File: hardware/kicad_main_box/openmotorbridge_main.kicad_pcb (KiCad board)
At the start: 4 copper layers, 85 x 55 mm, 41 parts, among them J1 DEUTSCH_DTM12_IDC_HEADER, J2 MicroSD_Card, J3 USB2_IDC_HEADER_9PIN, J4 RGB_LED_3PIN, J5 PWR_BAT_NTC_4PIN, SW1 SW_PAIR_RESET, U1 LM5164-Q1, U10 SX1262IMLTRT, U11 TPS7A0533_LDO, U2 ESP32-S3-WROOM-1U-N16R8, U3 ES8388_Codec, U5 BMI270_IMU, U6 TCAN334G, U8 DW3110, U9 QCC3084_BT54_AUDIO, Y1_UWB 38.4MHz

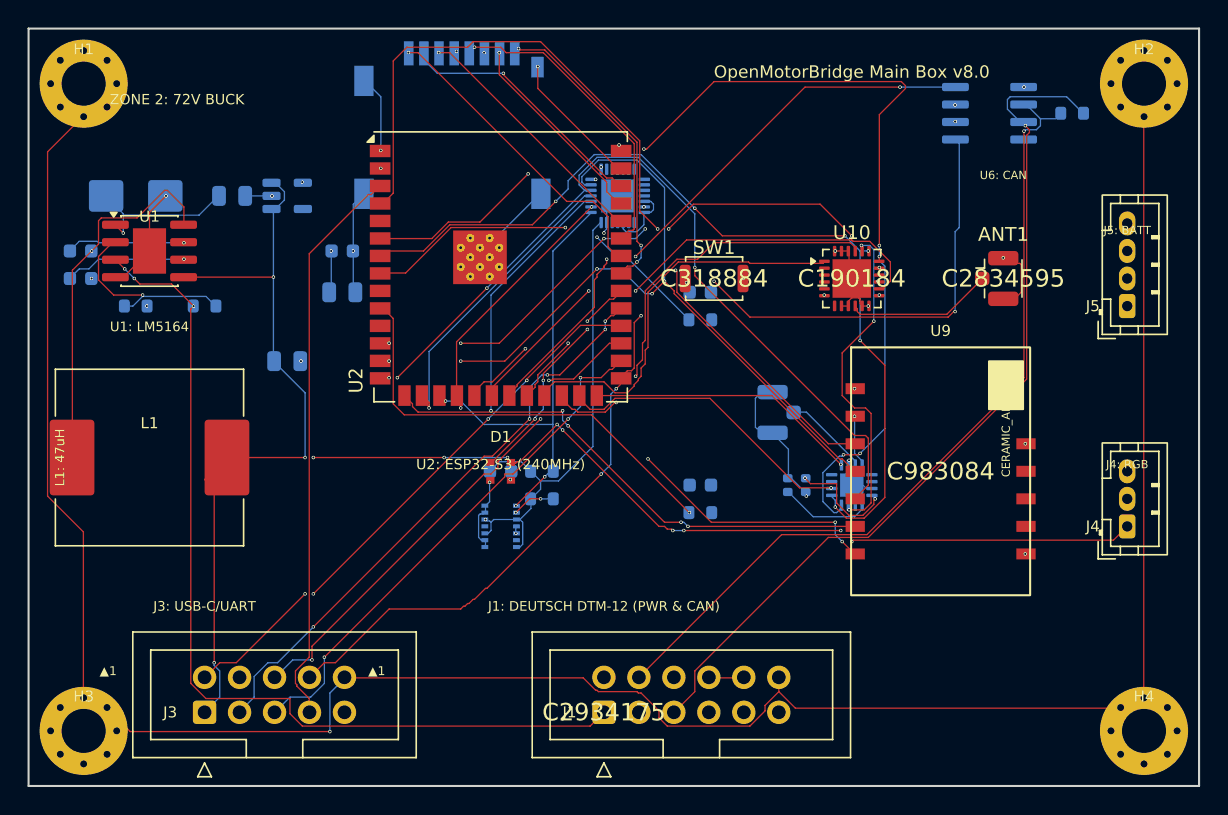
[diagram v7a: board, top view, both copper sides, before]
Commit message: feat(hw): finalize PCB lineup routing, sync PCBA 03 cartridge with J_PROG header and DTM12 schematics
- PCBA 01 (Central Box): Remediate net routing, DTM12 hierarchical schematic synchronization, 100% routed, 0 DRC errors.
- PCBA 03 (Smart Modular Cartridge): Position and route J_PROG 4-pin SMD programming header on F.Cu at (108.0, 89.61), synchronize CPL and schematic, 100% routed, 0 DRC errors.
- PCBA 05 (Universal Front Node): Preconnect and routing verified, 100% routed, 0 DRC errors.
- PCBA 07 (LoRa Smart-Keyfob): Routing and DRC verified, 100% routed, 0 DRC errors.
- PCBA 08 (Radar 2.0 Sub-MCU & Wings): Sub-MCU routing and HF isolation verified, 100% routed, 0 DRC errors.
- PCBA 10 (OMM 446 PMR/DMR Intercom): KiCad DRC verified, 100% routed, 0 DRC errors.
- Firmware: Align configuration headers across front_node and smart_cartridge.
- Tools: Add comprehensive preflight PCBA audit suite tools/audit_pcbas_preflight.py.
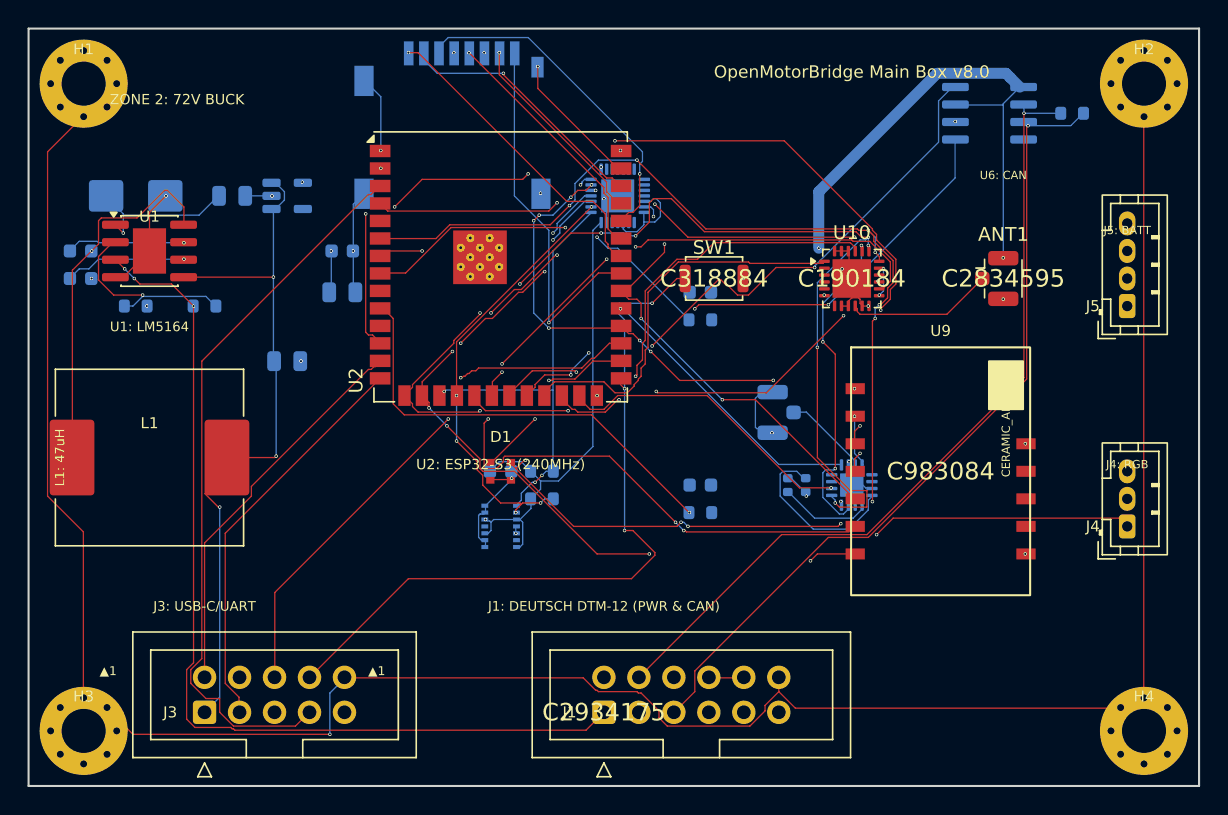
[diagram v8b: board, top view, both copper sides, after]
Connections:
- U2 pad 13: I2S_BCLK -> USB_D_N
- U2 pad 14: I2S_WS -> USB_D_P
- U2 pad 26: UWB_IRQ -> GND_PWR
- U2 pad 28: UART_TXD0 -> RGB_LED_DATA
- U2 pad 30: USB_D_N -> I2S_BCLK
- U2 pad 31: USB_D_P -> UWB_IRQ
- U2 pad 32: RGB_LED_DATA -> I2S_WS
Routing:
- net UART_TXD0: track 38.1 -> 0.00 mm, vias 3 -> 0
- net I2S_WS: track 59.0 -> 35.6 mm
- net I2S_MCLK: track 50.1 -> 71.5 mm, vias 6 -> 7
- net SPI_SCK: track 79.7 -> 61.7 mm
- net I2S_BCLK: track 58.8 -> 41.2 mm, vias 5 -> 9
- net GND_PWR: track 80.3 -> 95.9 mm, vias 23 -> 25
- net USB_D_P: track 42.4 -> 29.4 mm, vias 5 -> 0
- net USB_D_N: track 40.9 -> 28.5 mm, vias 4 -> 0
- net SPI_MISO: track 78.9 -> 66.6 mm, vias 6 -> 8
- net ESP_EN: track 40.8 -> 52.4 mm
- net ESP_BOOT: track 44.0 -> 54.7 mm, vias 4 -> 3
- net CAN_RX: track 49.0 -> 40.7 mm, vias 3 -> 4
- net SD_CMD: track 18.1 -> 24.4 mm
- net SD_DAT1: track 21.9 -> 27.3 mm, vias 3 -> 1
- net I2S_DOUT: track 55.9 -> 61.1 mm, vias 5 -> 8
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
